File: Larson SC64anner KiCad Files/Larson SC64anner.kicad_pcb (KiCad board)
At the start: 2 copper layers, 390 x 20 mm, 104 parts, among them J1 2x03, J10 2x03, J11 2x03, J12 2x03, J13 2x03, J14 2x03, J15 2x03, J16 2x03, J17 2x03, J18 2x03, J19 2x03, J2 2x03, J20 2x03, J21 1x02, J22 1x02, J23 1x01, J24 1x01, J25 1x01, J26 1x01, J29 1x01, J3 2x03, J30 1x01, J31 1x01, J32 1x01, J35 1x01, J36 1x01, J38 1x01, J4 2x03, J5 2x03, J6 2x03, J7 2x03, J8 2x03, J9 2x03, U1 ATtiny85V-20PU, U2 NE555, U3 SN74LVC2GU04DCKR, U4 LM386N-4_NOPB, U5 LM386N-4_NOPB

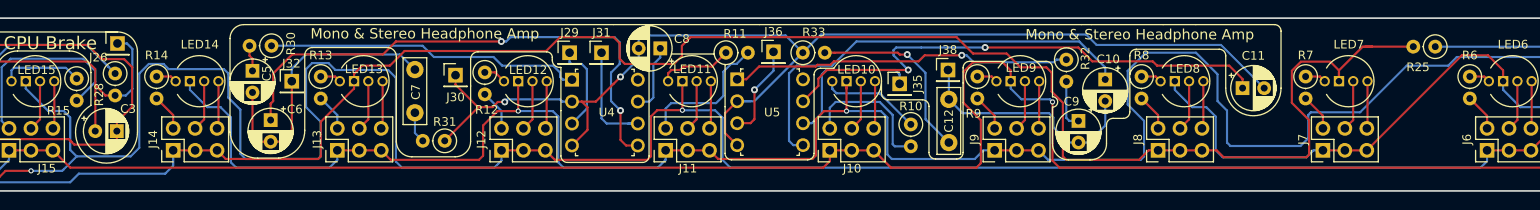
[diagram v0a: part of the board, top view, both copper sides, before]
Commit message: Re-arrange headphone amp circtuit
Re-did and re-arranged the whole headphone amp circuitry into a more orderly fashion.
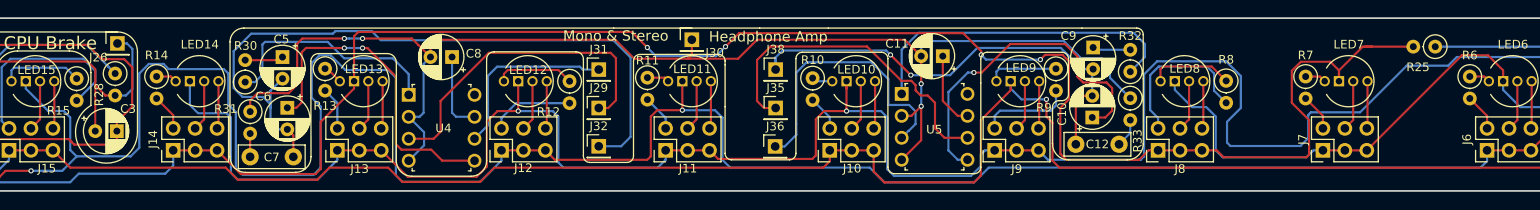
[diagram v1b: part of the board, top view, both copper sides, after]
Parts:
- moved R33 38.3 mm to (258.7, 29.3), turned to 270 degrees
- moved J32 36.3 mm to (197.2, 34.8)
- moved C11 34.9 mm to (237.0, 24.4), turned to 180 degrees
- moved J30 27.7 mm to (207.9, 22.5)
- moved C8 24.1 mm to (180.2, 24.5)
- moved R31 22.8 mm to (156.8, 30.8), turned to 270 degrees
- moved J38 20.0 mm to (217.7, 25.9)
- moved U5 19.1 mm to (232.2, 28.8)
- moved U4 19.0 mm to (175.2, 28.9)
- moved C7 17.3 mm to (161.8, 36.0), turned to 180 degrees
- moved C12 15.6 mm to (252.4, 34.6), turned to 0 degrees
- moved J35 14.6 mm to (217.7, 30.4)
- moved R10 12.6 mm to (221.9, 26.9)
- moved J36 11.0 mm to (217.6, 34.9)
- moved R12 9.86 mm to (193.8, 27.3)
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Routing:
- net Net-(C11-Pad1): track 60.3 -> 8.76 mm, vias 2 -> 0
- net Net-(C5-Pad2): track 33.0 -> 82.6 mm
- net Net-(J29-Pad1): track 10.4 -> 37.7 mm
- net Net-(C10-Pad2): track 27.9 -> 53.7 mm, vias 0 -> 2
- net Net-(C6-Pad1): track 62.0 -> 37.9 mm
- net Net-(J36-Pad1): track 10.9 -> 32.3 mm, vias 1 -> 0
- net Net-(J35-Pad1): track 17.7 -> 38.7 mm
- net Net-(C12-Pad2): track 21.8 -> 3.34 mm, vias 1 -> 0
- net Net-(C11-Pad2): track 134.4 -> 152.2 mm, vias 2 -> 4
- net Net-(J8-Pad2): track 4.26 -> 18.7 mm
- net Net-(J10-Pad2): track 16.2 -> 4.10 mm
- net Net-(J11-Pad2): track 16.1 -> 4.20 mm
- net Net-(C10-Pad1): track 50.4 -> 39.4 mm, vias 0 -> 1
- net Net-(R30-Pad1): track 36.7 -> 26.8 mm
- net Net-(LED10-Pad1): track 11.7 -> 2.43 mm
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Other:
- board text added: "Headphone Amp"
- board text added: "Mono & Stereo"
- board text removed: "Mono & Stereo Headphone Amp"

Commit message: Updated PCB, README, Schmetic
Simpliefied things a bit.
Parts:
- removed J30: 1x01, Connector_PinHeader_2.54mm:PinHeader_1x01_P2.54mm_Vertical
- J26: value 1x01 -> 2x05; footprint Connector_PinHeader_2.54mm:PinHeader_1x01_P2.54mm_Vertical -> Connector_PinHeader_2.54mm:PinHeader_2x05_P2.54mm_Vertical
- R1, R10, R11, R12, R13, R14, R15, R16, R17, R18, R19, R2, R20, R21, R22, R23, R24, R25, R26, R27, R28, R3, R30, R31, R32, R33, R4, R5, R6, R7, R8, R9: footprint Resistor_THT:R_Axial_DIN0207_L6.3mm_D2.5mm_P2.54mm_Vertical -> libraries:R_Axial_DIN0207_L6.3mm_D2.5mm_P2.54mm_Vertical_reduced_courtyard
- U4, U5: footprint digikey-footprints:DIP-8_W7.62mm -> Package_DIP:DIP-8_W7.62mm
- moved J26 131.4 mm to (272.9, 23.4)
- moved J21 2.55 mm to (412.4, 23.3), turned to 90 degrees
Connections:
- C3 pad 1: Net-(C3-Pad1) -> Net-(C11-Pad2)
- J21 pad 2: Net-(J21-Pad2) -> Net-(J21-Pad1)
- J26 pad 1: Net-(C3-Pad1) -> Net-(C11-Pad2)
- R28 pad 2: Net-(C3-Pad1) -> Net-(C11-Pad2)
- U1 pad 4: Net-(J21-Pad1) -> Net-(C11-Pad2)
- U1 pad 8: Net-(J21-Pad2) -> Net-(J21-Pad1)
- U2 pad 2: Net-(C3-Pad1) -> Net-(C11-Pad2)
- U2 pad 6: Net-(C3-Pad1) -> Net-(C11-Pad2)
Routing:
- net Net-(C11-Pad2): track 152.2 -> 382.8 mm, vias 4 -> 5
- net Net-(C3-Pad1): track 45.0 -> 0.00 mm
- net Net-(J21-Pad2): track 6.48 -> 0.00 mm
- net Net-(J21-Pad1): track 13.4 -> 9.02 mm
- net Net-(J11-Pad1): track 360.7 -> 362.7 mm
- added copper zone on F.Cu, net Net-(C11-Pad2)

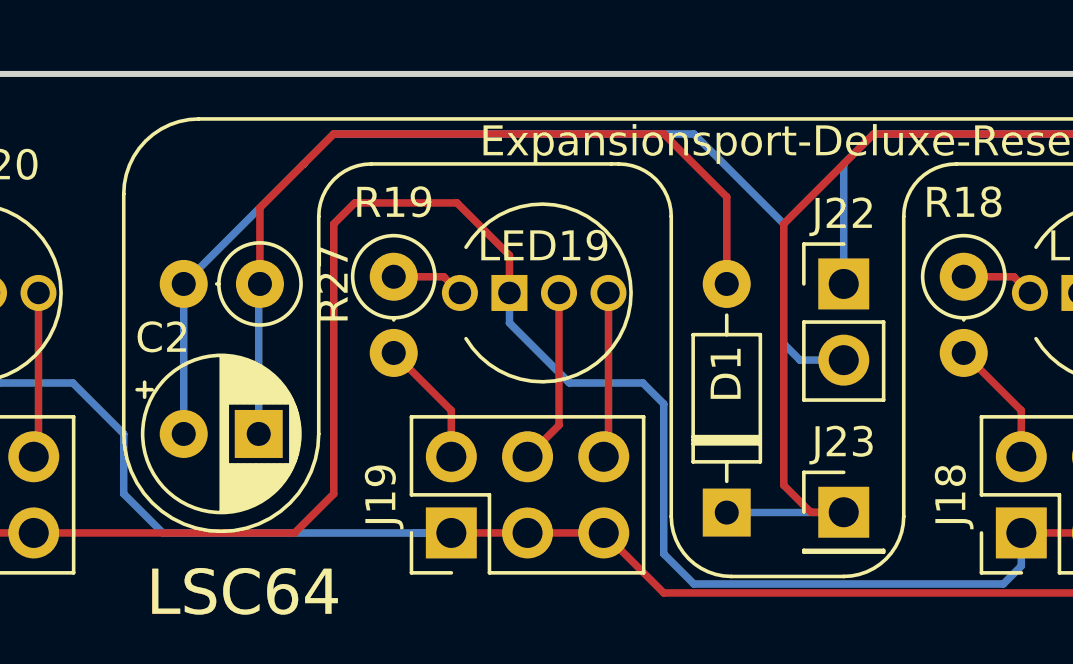
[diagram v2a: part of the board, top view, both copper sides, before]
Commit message: Updated README
Switched the description of the connections from stupid text lists to tables. Much better!
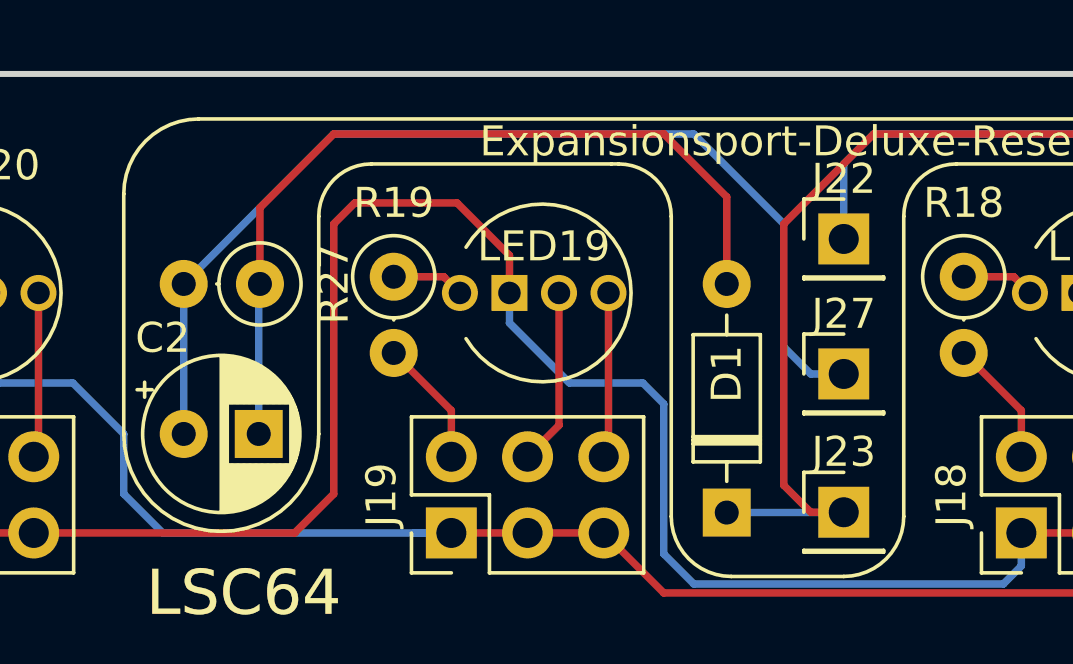
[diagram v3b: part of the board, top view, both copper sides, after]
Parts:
- added J27: 1x01, Connector_PinHeader_2.54mm:PinHeader_1x01_P2.54mm_Vertical, F.Cu at (66.0, 30.0)
- J22: value 1x02 -> 1x01; footprint Connector_PinHeader_2.54mm:PinHeader_1x02_P2.54mm_Vertical -> Connector_PinHeader_2.54mm:PinHeader_1x01_P2.54mm_Vertical
- moved J22 1.50 mm to (66.0, 25.5)
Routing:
- net Net-(C1-Pad1): track 30.1 -> 28.6 mm
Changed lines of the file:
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@@
     (thickness 1.6)
     (drawings 157)
-    (tracks 1025)
+    (tracks 1024)
     (zones 0)
-    (modules 103)
+    (modules 104)
     (nets 120)
   )
@@
     )
   )
-  (module Connector_PinHeader_2.54mm:PinHeader_1x02_P2.54mm_Vertical (layer F.Cu)
-    (at 66 27)
-    (descr "Through hole straight pin header, 1x02, 2.54mm pitch, single row")
-    (tags "Through hole pin header THT 1x02 2.54mm single row")
-    (fp_text reference J22 (at 0 -2.33) (layer F.SilkS)
-      (effects (font (size 1 1) (thickness 0.15)))
-    )
-    (fp_text value 1x02 (at 3 -2) (layer F.Fab)
-      (effects (font (size 1 1) (thickness 0.15)))
-    )
-    (fp_line (start -0.635 -1.27) (end 1.27 -1.27) (layer F.Fab) (width 0.1))
-    (fp_line (start 1.27 -1.27) (end 1.27 3.81) (layer F.Fab) (width 0.1))
-    (fp_line (start 1.27 3.81) (end -1.27 3.81) (layer F.Fab) (width 0.1))
-    (fp_line (start -1.27 3.81) (end -1.27 -0.635) (layer F.Fab) (width 0.1))
-    (fp_line (start -1.27 -0.635) (end -0.635 -1.27) (layer F.Fab) (width 0.1))
-    (fp_line (start -1.33 3.87) (end 1.33 3.87) (layer F.SilkS) (width 0.12))
-    (fp_line (start -1.33 1.27) (end -1.33 3.87) (layer F.SilkS) (width 0.12))
-    (fp_line (start 1.33 1.27) (end 1.33 3.87) (layer F.SilkS) (width 0.12))
-    (fp_line (start -1.33 1.27) (end 1.33 1.27) (layer F.SilkS) (width 0.12))
-    (fp_line (start -1.33 0) (end -1.33 -1.33) (layer F.SilkS) (width 0.12))
-    (fp_line (start -1.33 -1.33) (end 0 -1.33) (layer F.SilkS) (width 0.12))
-    (fp_line (start -1.8 -1.8) (end -1.8 4.35) (layer F.CrtYd) (width 0.05))
-    (fp_line (start -1.8 4.35) (end 1.8 4.35) (layer F.CrtYd) (width 0.05))
-    (fp_line (start 1.8 4.35) (end 1.8 -1.8) (layer F.CrtYd) (width 0.05))
-    (fp_line (start 1.8 -1.8) (end -1.8 -1.8) (layer F.CrtYd) (width 0.05))
-    (fp_text user %R (at 0 1.27 -270) (layer F.Fab)
-      (effects (font (size 1 1) (thickness 0.15)))
-    )
-    (pad 1 thru_hole rect (at 0 0) (size 1.7 1.7) (drill 1) (layers *.Cu *.Mask)
-      (net 92 "Net-(C1-Pad1)"))
-    (pad 2 thru_hole oval (at 0 2.54) (size 1.7 1.7) (drill 1) (layers *.Cu *.Mask)
-      (net 93 "Net-(C2-Pad1)"))
-    (model ${KISYS3DMOD}/Connector_PinHeader_2.54mm.3dshapes/PinHeader_1x02_P2.54mm_Vertical.wrl
-      (at (xyz 0 0 0))
-      (scale (xyz 1 1 1))
-      (rotate (xyz 0 0 0))
-    )
-  )
   (module Connector_PinHeader_2.54mm:PinHeader_1x01_P2.54mm_Vertical (layer F.Cu)
     (at 66 34.61)
     (descr "Through hole straight pin header, 1x01, 2.54mm pitch, single row")
     (tags "Through hole pin header THT 1x01 2.54mm single row")
-    (fp_text reference J23 (at 0 -2.33) (layer F.SilkS)
+    (fp_text reference J23 (at 0 -2.01) (layer F.SilkS)
       (effects (font (size 1 1) (thickness 0.15)))
     )
@@
     )
   )
+  (module Connector_PinHeader_2.54mm:PinHeader_1x01_P2.54mm_Vertical (layer F.Cu)
+    (at 66 25.5)
+    (descr "Through hole straight pin header, 1x01, 2.54mm pitch, single row")
+    (tags "Through hole pin header THT 1x01 2.54mm single row")
+    (fp_text reference J22 (at 0 -2) (layer F.SilkS)
+      (effects (font (size 1 1) (thickness 0.15)))
+    )
+    (fp_text value 1x01 (at 0 2.33) (layer F.Fab)
+      (effects (font (size 1 1) (thickness 0.15)))
+    )
+    (fp_text user %R (at 0 0 90) (layer F.Fab)
+      (effects (font (size 1 1) (thickness 0.15)))
+    )
+    (fp_line (start 1.8 -1.8) (end -1.8 -1.8) (layer F.CrtYd) (width 0.05))
+    (fp_line (start 1.8 1.8) (end 1.8 -1.8) (layer F.CrtYd) (width 0.05))
+    (fp_line (start -1.8 1.8) (end 1.8 1.8) (layer F.CrtYd) (width 0.05))
+    (fp_line (start -1.8 -1.8) (end -1.8 1.8) (layer F.CrtYd) (width 0.05))
+    (fp_line (start -1.33 -1.33) (end 0 -1.33) (layer F.SilkS) (width 0.12))
+    (fp_line (start -1.33 0) (end -1.33 -1.33) (layer F.SilkS) (width 0.12))
+    (fp_line (start -1.33 1.27) (end 1.33 1.27) (layer F.SilkS) (width 0.12))
+    (fp_line (start 1.33 1.27) (end 1.33 1.33) (layer F.SilkS) (width 0.12))
+    (fp_line (start -1.33 1.27) (end -1.33 1.33) (layer F.SilkS) (width 0.12))
+    (fp_line (start -1.33 1.33) (end 1.33 1.33) (layer F.SilkS) (width 0.12))
+    (fp_line (start -1.27 -0.635) (end -0.635 -1.27) (layer F.Fab) (width 0.1))
+    (fp_line (start -1.27 1.27) (end -1.27 -0.635) (layer F.Fab) (width 0.1))
+    (fp_line (start 1.27 1.27) (end -1.27 1.27) (layer F.Fab) (width 0.1))
+    (fp_line (start 1.27 -1.27) (end 1.27 1.27) (layer F.Fab) (width 0.1))
+    (fp_line (start -0.635 -1.27) (end 1.27 -1.27) (layer F.Fab) (width 0.1))
+    (pad 1 thru_hole rect (at 0 0) (size 1.7 1.7) (drill 1) (layers *.Cu *.Mask)
+      (net 92 "Net-(C1-Pad1)"))
+    (model ${KISYS3DMOD}/Connector_PinHeader_2.54mm.3dshapes/PinHeader_1x01_P2.54mm_Vertical.wrl
+      (at (xyz 0 0 0))
+      (scale (xyz 1 1 1))
+      (rotate (xyz 0 0 0))
+    )
+  )
+  (module Connector_PinHeader_2.54mm:PinHeader_1x01_P2.54mm_Vertical (layer F.Cu)
+    (at 66 30)
+    (descr "Through hole straight pin header, 1x01, 2.54mm pitch, single row")
+    (tags "Through hole pin header THT 1x01 2.54mm single row")
+    (fp_text reference J27 (at 0 -2) (layer F.SilkS)
+      (effects (font (size 1 1) (thickness 0.15)))
+    )
+    (fp_text value 1x01 (at 0 2.33) (layer F.Fab)
+      (effects (font (size 1 1) (thickness 0.15)))
+    )
+    (fp_line (start -0.635 -1.27) (end 1.27 -1.27) (layer F.Fab) (width 0.1))
+    (fp_line (start 1.27 -1.27) (end 1.27 1.27) (layer F.Fab) (width 0.1))
+    (fp_line (start 1.27 1.27) (end -1.27 1.27) (layer F.Fab) (width 0.1))
+    (fp_line (start -1.27 1.27) (end -1.27 -0.635) (layer F.Fab) (width 0.1))
+    (fp_line (start -1.27 -0.635) (end -0.635 -1.27) (layer F.Fab) (width 0.1))
+    (fp_line (start -1.33 1.33) (end 1.33 1.33) (layer F.SilkS) (width 0.12))
+    (fp_line (start -1.33 1.27) (end -1.33 1.33) (layer F.SilkS) (width 0.12))
+    (fp_line (start 1.33 1.27) (end 1.33 1.33) (layer F.SilkS) (width 0.12))
+    (fp_line (start -1.33 1.27) (end 1.33 1.27) (layer F.SilkS) (width 0.12))
+    (fp_line (start -1.33 0) (end -1.33 -1.33) (layer F.SilkS) (width 0.12))
+    (fp_line (start -1.33 -1.33) (end 0 -1.33) (layer F.SilkS) (width 0.12))
+    (fp_line (start -1.8 -1.8) (end -1.8 1.8) (layer F.CrtYd) (width 0.05))
+    (fp_line (start -1.8 1.8) (end 1.8 1.8) (layer F.CrtYd) (width 0.05))
+    (fp_line (start 1.8 1.8) (end 1.8 -1.8) (layer F.CrtYd) (width 0.05))
+    (fp_line (start 1.8 -1.8) (end -1.8 -1.8) (layer F.CrtYd) (width 0.05))
+    (fp_text user %R (at 0 0 90) (layer F.Fab)
+      (effects (font (size 1 1) (thickness 0.15)))
+    )
+    (pad 1 thru_hole rect (at 0 0) (size 1.7 1.7) (drill 1) (layers *.Cu *.Mask)
+      (net 93 "Net-(C2-Pad1)"))
+    (model ${KISYS3DMOD}/Connector_PinHeader_2.54mm.3dshapes/PinHeader_1x01_P2.54mm_Vertical.wrl
+      (at (xyz 0 0 0))
+      (scale (xyz 1 1 1))
+      (rotate (xyz 0 0 0))
+    )
+  )
   (gr_line (start 201.2 24.95) (end 201.2 26.15) (layer F.SilkS) (width 0.12))
   (gr_line (start 205.15 24.2) (end 201.95 24.2) (layer F.SilkS) (width 0.12))
@@
   (segment (start 67 22) (end 66 23) (width 0.25) (layer B.Cu) (net 92))
   (segment (start 81.5 22) (end 67 22) (width 0.25) (layer B.Cu) (net 92))
-  (segment (start 66 23) (end 66 27) (width 0.25) (layer B.Cu) (net 92))
   (segment (start 82 27) (end 82 22.5) (width 0.25) (layer B.Cu) (net 92))
   (segment (start 82 22.5) (end 81.5 22) (width 0.25) (layer B.Cu) (net 92))
+  (segment (start 66 23) (end 66 25.5) (width 0.25) (layer B.Cu) (net 92))
   (segment (start 44 32) (end 44 27) (width 0.25) (layer B.Cu) (net 93))
-  (segment (start 48 23) (end 44 27) (width 0.25) (layer B.Cu) (net 93))
-  (segment (start 64 25) (end 61 22) (width 0.25) (layer B.Cu) (net 93))
-  (segment (start 66 29.54) (end 64.54 29.54) (width 0.25) (layer B.Cu) (net 93))
-  (segment (start 61 22) (end 49 22) (width 0.25) (layer B.Cu) (net 93))
-  (segment (start 49 22) (end 48 23) (width 0.25) (layer B.Cu) (net 93))
-  (segment (start 64 29) (end 64 25) (width 0.25) (layer B.Cu) (net 93))
-  (segment (start 64.54 29.54) (end 64 29) (width 0.25) (layer B.Cu) (net 93))
+  (segment (start 64.9 30) (end 66 30) (width 0.25) (layer B.Cu) (net 93))
+  (segment (start 44 27) (end 49 22) (width 0.25) (layer B.Cu) (net 93))
+  (segment (start 61 22) (end 64 25) (width 0.25) (layer B.Cu) (net 93))
+  (segment (start 49 22) (end 61 22) (width 0.25) (layer B.Cu) (net 93))
+  (segment (start 64 25) (end 64 29.1) (width 0.25) (layer B.Cu) (net 93))
+  (segment (start 64 29.1) (end 64.9 30) (width 0.25) (layer B.Cu) (net 93))
   (segment (start 46.5 27.04) (end 46.54 27) (width 0.25) (layer B.Cu) (net 94))
   (segment (start 46.5 32) (end 46.5 27.04) (width 0.25) (layer B.Cu) (net 94))

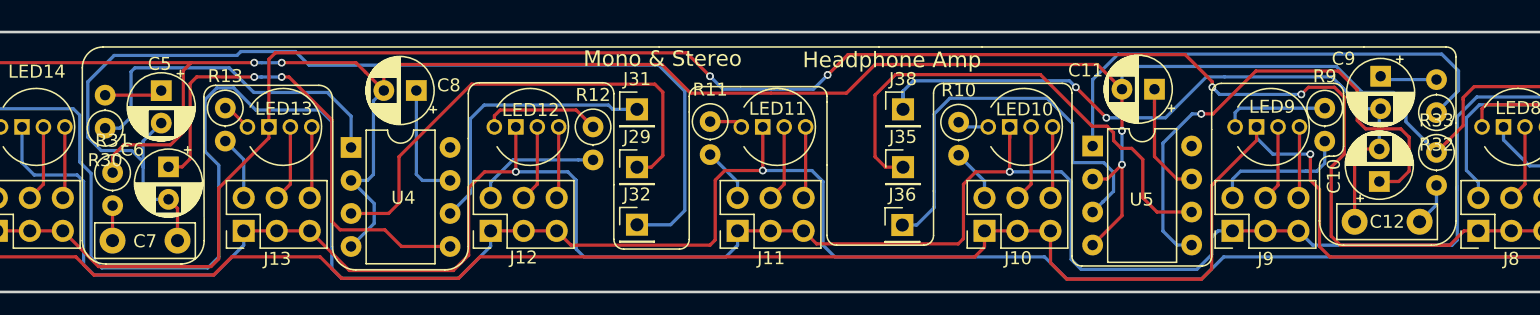
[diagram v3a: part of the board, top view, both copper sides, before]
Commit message: Cleanup and corrections
Cleaned up the pcb a bit and made new screenshots.
Also fixed some more minor things in the README. Will it ever end? :D
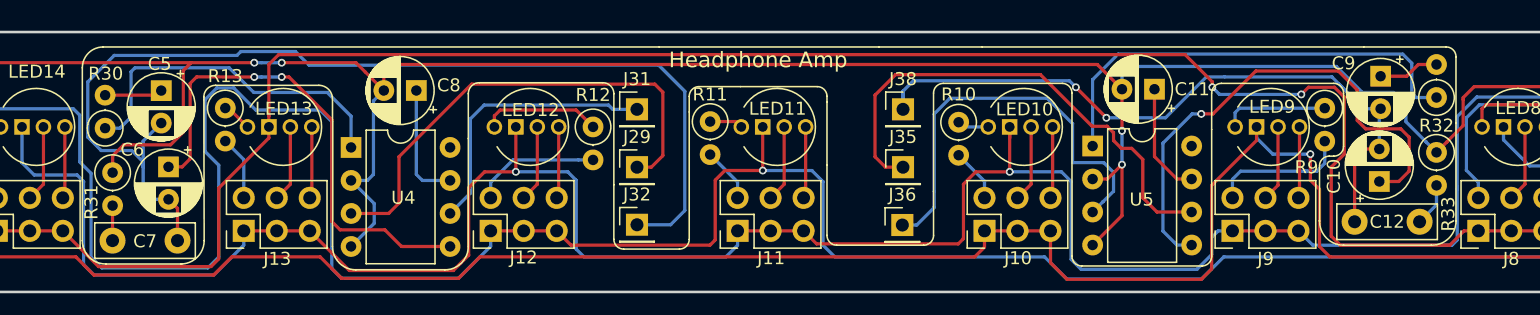
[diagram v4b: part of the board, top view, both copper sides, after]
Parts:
- moved R32 1.16 mm to (258.7, 25.0)
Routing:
- net Net-(R32-Pad1): track 38.5 -> 35.1 mm
- net Net-(J14-Pad1): track 360.0 -> 357.4 mm, vias 4 -> 2
- net Net-(C11-Pad2): track 382.8 -> 381.0 mm
- net Net-(C9-Pad1): track 4.41 -> 5.04 mm
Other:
- board text removed: "Mono & Stereo"
